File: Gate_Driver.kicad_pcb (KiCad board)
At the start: 2 copper layers, 110.3 x 47.3 mm, 23 parts

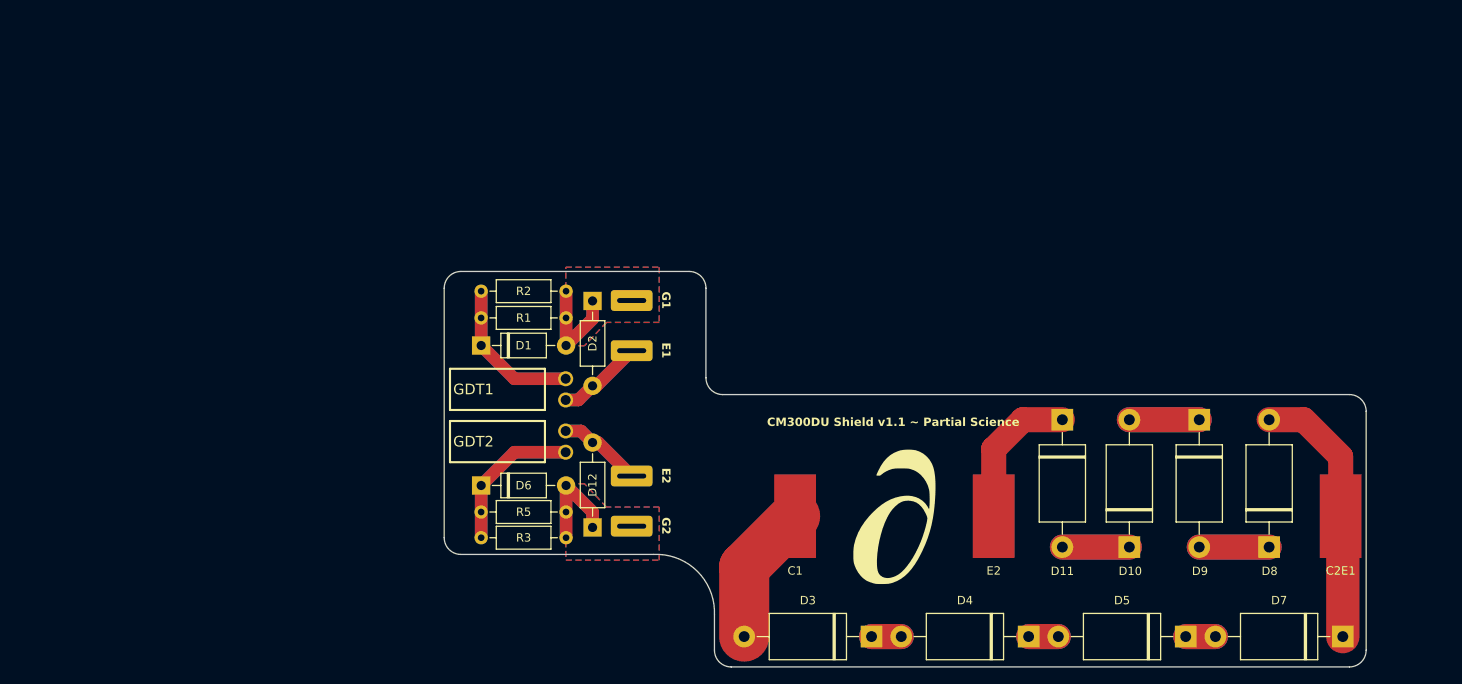
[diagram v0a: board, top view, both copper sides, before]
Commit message: Design done with smaller cap
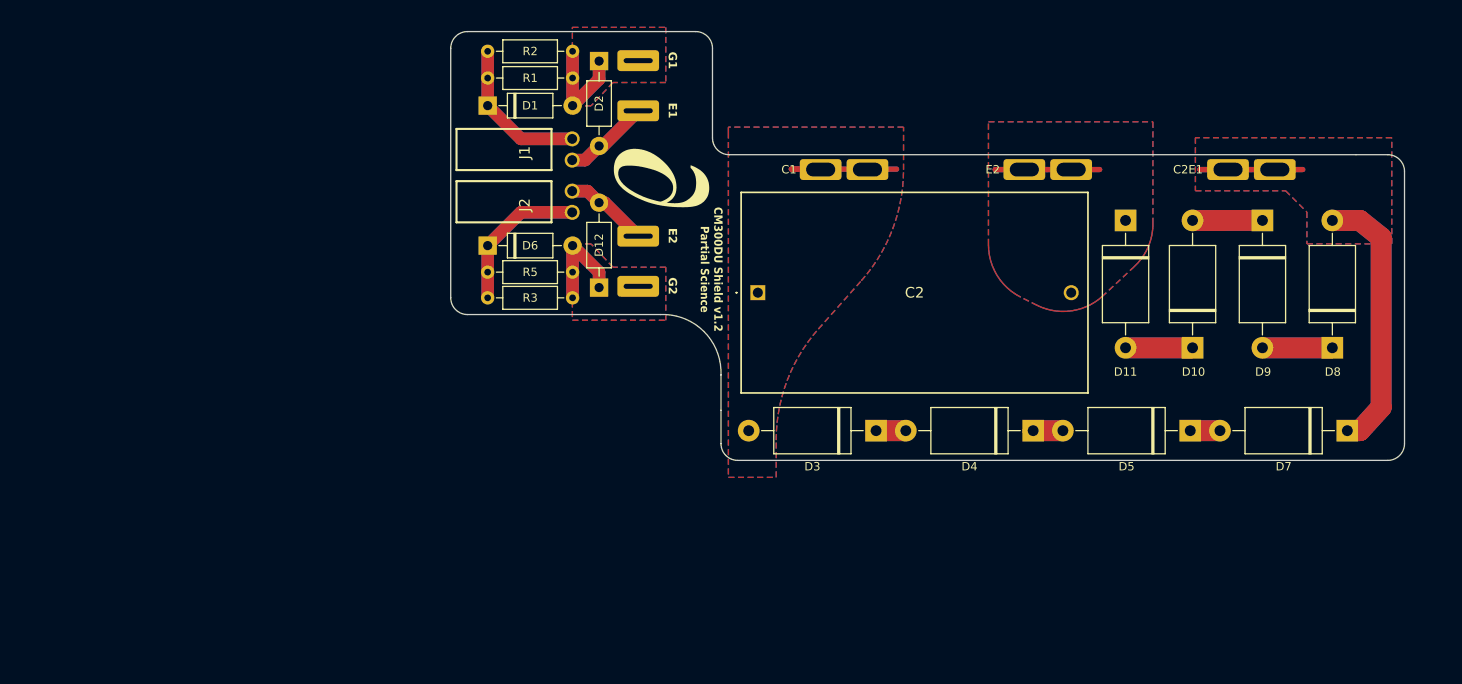
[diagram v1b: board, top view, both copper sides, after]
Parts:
- added C2: B32776T1275K000, SamacSys_Parts:B32776T1275K000, F.Cu at (121.8, 106.7)
- C1, C2E1, E2: footprint Connector_Wire:SolderWirePad_1x01_SMD_5x10mm -> Library:Custom CM300DU Terminal Connector
- D12, D2: value D_Zener -> P6KE30CA
- moved G*** 48.9 mm to (110.3, 93.0), turned to -90 degrees
- moved C2E1 42.8 mm to (180.8, 91.9)
- moved E2 42.0 mm to (156.5, 91.9)
- moved C1 41.9 mm to (132.1, 91.9)
- moved D12 28.7 mm to (102.8, 106.1)
- moved R5 28.7 mm to (89.5, 104.2)
- moved D1 28.7 mm to (89.5, 84.3)
- moved D2 28.7 mm to (102.8, 79.0)
- moved D6 28.7 mm to (89.5, 101.0)
- moved J1 28.7 mm to (93.9, 89.5)
- moved J2 28.7 mm to (93.9, 95.8)
- moved Q1 28.7 mm to (107.5, 92.4)
- moved R1 28.7 mm to (89.5, 81.0)
- moved R2 28.7 mm to (89.5, 77.8)
- moved R3 28.7 mm to (89.5, 107.3)
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- renumbered GDT1 to J1, GDT2 to J2
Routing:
- net Net-(C2E1-Pin_1): track 32.0 -> 0.00 mm
- net Net-(D11-A1): track 17.7 -> 0.00 mm
- net Net-(C1-Pin_1): track 16.9 -> 0.00 mm
- net Net-(D8-A1): track 16.7 -> 0.00 mm
- net Net-(D10-A2): track 16.7 -> 0.00 mm
- net Net-(D10-A1): track 16.0 -> 0.00 mm
- net Net-(D5-A1): track 7.11 -> 0.00 mm
- net Net-(D4-A1): track 7.11 -> 0.00 mm
- net Net-(D3-A1): track 7.11 -> 0.00 mm
- added copper zone on B.Cu, net Net-(C1-Pin_1)
- added copper zone on F.Cu, net Net-(C1-Pin_1)
- added copper zone on B.Cu, net Net-(C2E1-Pin_1)
- added copper zone on F.Cu, net Net-(C2E1-Pin_1)
- added copper zone on B.Cu, net Net-(D11-A1)
- added copper zone on F.Cu, net Net-(D11-A1)
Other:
- board size 110.3 x 47.3 mm -> 114.1 x 51.3 mm
- board text added: "CM300DU Shield v1.2 Partial Science"
- board text removed: "CM300DU Shield v1.1 ~ Partial Science"

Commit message: minor tweaks
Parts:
- removed C2: B32776T1275K000, SamacSys_Parts:B32776T1275K000
- moved G*** 62.4 mm to (48.3, 100.3), turned to 0 degrees
- moved C2E1 22.2 mm to (198.8, 105.0)
- moved C1 13.2 mm to (133.5, 105.0)
- moved E2 13.1 mm to (157.3, 105.0)
- moved D5 7.68 mm to (180.2, 119.4)
- moved D3 7.68 mm to (142.6, 119.4)
- moved D4 7.68 mm to (161.4, 119.4)
- moved D7 7.68 mm to (199.0, 119.4)
- moved D1 6.48 mm to (95.9, 84.6)
- moved D12 6.48 mm to (109.3, 106.4)
- moved D2 6.48 mm to (109.3, 79.3)
- moved D6 6.48 mm to (95.9, 101.4)
- moved R1 6.48 mm to (95.9, 81.3)
- moved R2 6.48 mm to (95.9, 78.1)
- moved R3 6.48 mm to (95.9, 107.6)
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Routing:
- net Net-(C2E1-Pin_1): track 0.00 -> 32.0 mm
- net Net-(D11-A1): track 0.00 -> 17.7 mm
- net Net-(C1-Pin_1): track 0.00 -> 16.9 mm
- net Net-(D8-A1): track 0.00 -> 16.7 mm
- net Net-(D10-A2): track 0.00 -> 16.7 mm
- net Net-(D10-A1): track 0.00 -> 16.0 mm
- net Net-(D4-A1): track 0.00 -> 7.11 mm
- net Net-(D3-A1): track 0.00 -> 7.11 mm
- net Net-(D5-A1): track 0.00 -> 7.11 mm
- removed copper zone on B.Cu, net Net-(C1-Pin_1)
- removed copper zone on F.Cu, net Net-(C1-Pin_1)
- removed copper zone on B.Cu, net Net-(C2E1-Pin_1)
- removed copper zone on F.Cu, net Net-(C2E1-Pin_1)
- removed copper zone on B.Cu, net Net-(D11-A1)
- removed copper zone on F.Cu, net Net-(D11-A1)
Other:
- board size 114.1 x 51.3 mm -> 110.3 x 47.3 mm
- board text added: "CM300DU Shield v1.1 ~ Partial Science"
- board text removed: "CM300DU Shield v1.2 Partial Science"

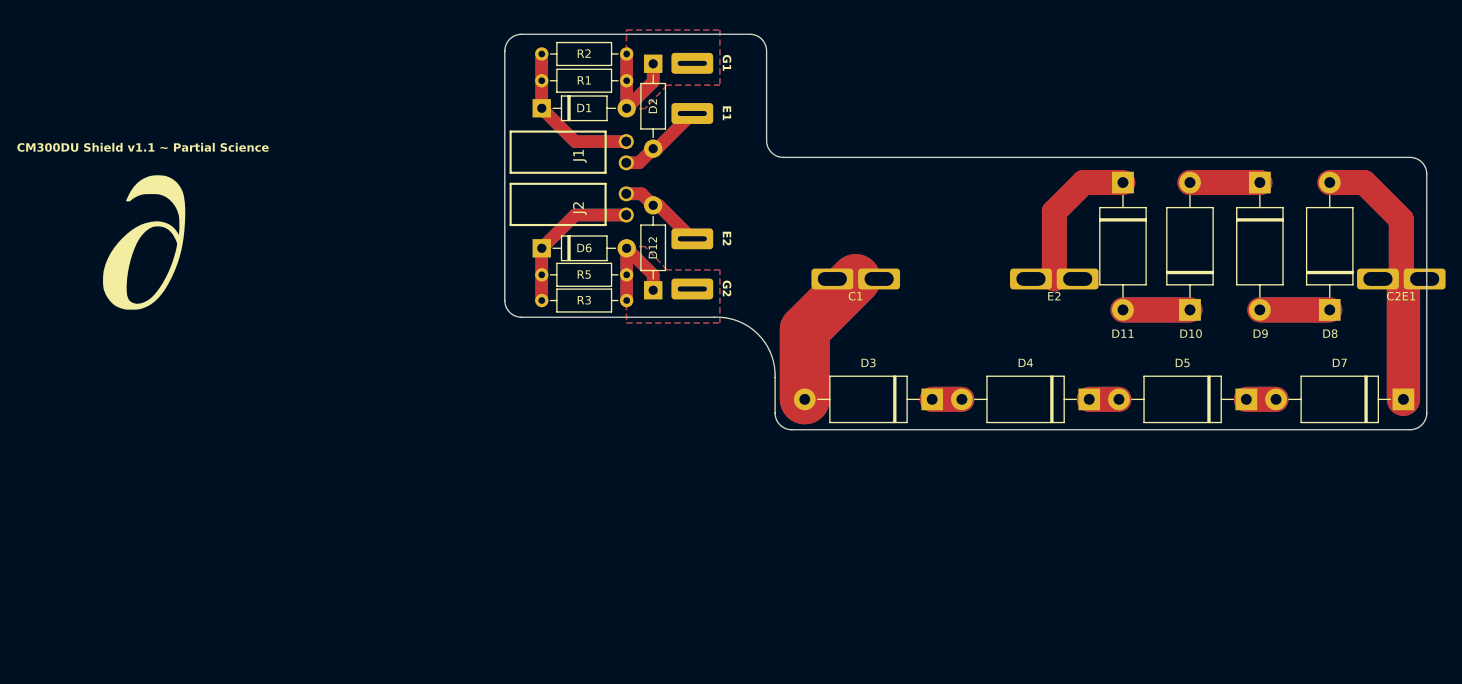
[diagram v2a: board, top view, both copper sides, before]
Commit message: Added pots and re-routed
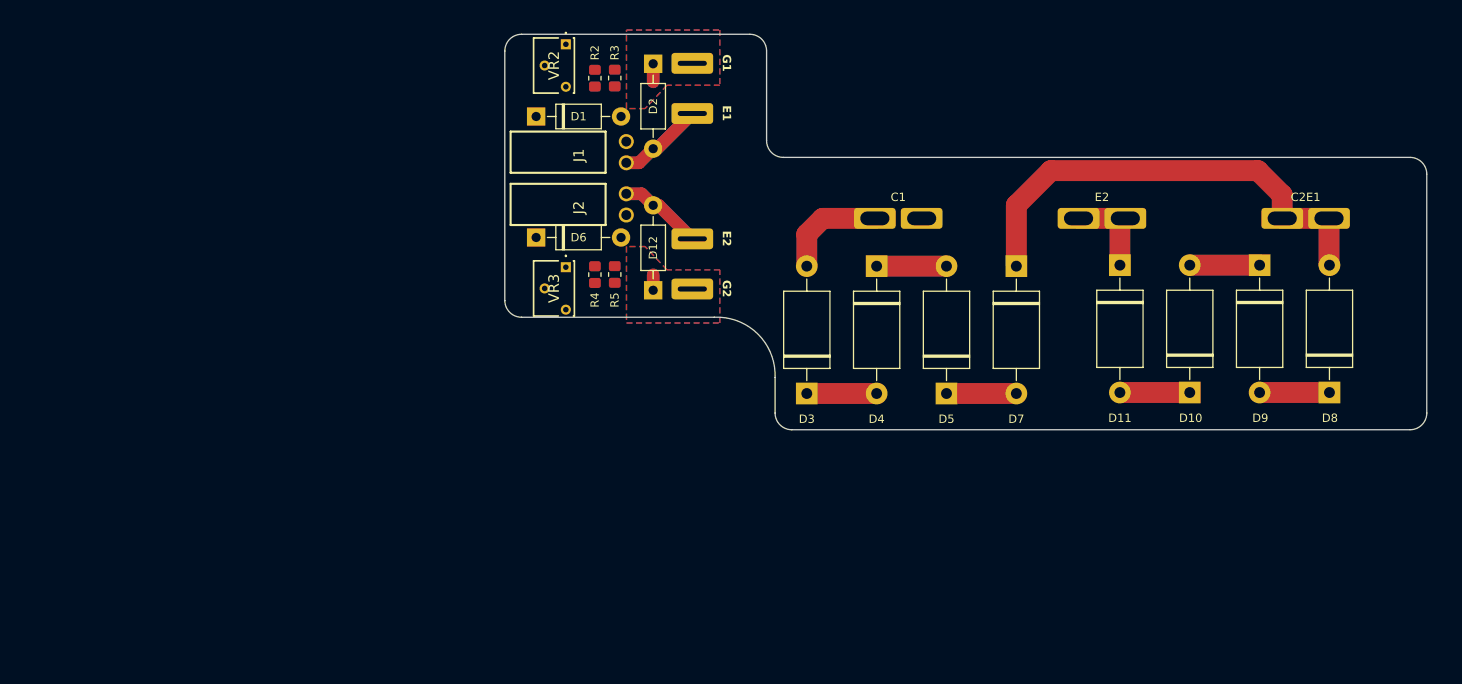
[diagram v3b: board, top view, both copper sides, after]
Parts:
- removed G***: LOGO, LOGO
- removed R1: 5.1, Resistor_THT:R_Axial_DIN0207_L6.3mm_D2.5mm_P10.16mm_Horizontal
- added R4: R, Resistor_SMD:R_0805_2012Metric_Pad1.20x1.40mm_HandSolder, F.Cu at (102.3, 104.5)
- added VR2: 3362X-1-100LF, SamacSys_Parts:3362X1100LF, F.Cu at (98.8, 77.0)
- added VR3: 3362X-1-100LF, SamacSys_Parts:3362X1100LF, F.Cu at (98.8, 103.6)
- R2, R3: footprint Resistor_THT:R_Axial_DIN0207_L6.3mm_D2.5mm_P10.16mm_Horizontal -> Resistor_SMD:R_0805_2012Metric_Pad1.20x1.40mm_HandSolder
- R5: value 5.1 -> R; footprint Resistor_THT:R_Axial_DIN0207_L6.3mm_D2.5mm_P10.16mm_Horizontal -> Resistor_SMD:R_0805_2012Metric_Pad1.20x1.40mm_HandSolder
- moved D7 49.0 mm to (152.7, 103.5), turned to -90 degrees
- moved D5 35.9 mm to (144.4, 118.7), turned to 90 degrees
- moved D4 30.0 mm to (136.0, 103.5), turned to -90 degrees
- moved R3 28.0 mm to (104.7, 81.0), turned to 90 degrees
- moved D3 15.0 mm to (127.6, 118.7), turned to 90 degrees
- moved C2E1 13.6 mm to (187.3, 97.8)
- moved D11 9.89 mm to (165.1, 103.4)
- moved D8 9.89 mm to (190.2, 118.6)
- moved D9 9.89 mm to (181.8, 103.4)
- moved D10 9.89 mm to (173.5, 118.6)
- moved E2 9.22 mm to (162.9, 97.8)
- moved C1 8.86 mm to (138.6, 97.8)
- moved R5 8.73 mm to (104.7, 104.5), turned to -90 degrees
- moved R2 6.98 mm to (102.3, 81.0), turned to 90 degrees
- moved D6 1.46 mm to (95.2, 100.1)
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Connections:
- R3 pad 1: Net-(D6-K) -> Net-(D1-K)
- R3 pad 2: Net-(D12-K) -> Net-(D1-A)
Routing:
- net Net-(D1-K): track 36.5 -> 0.00 mm
- net Net-(D6-K): track 36.0 -> 0.00 mm
- net Net-(C2E1-Pin_1): track 32.0 -> 56.0 mm
- net Net-(D1-A): track 26.3 -> 4.32 mm
- net Net-(D12-K): track 25.2 -> 3.70 mm
- net Net-(D10-A2): track 16.7 -> 8.36 mm
- net Net-(D8-A1): track 16.7 -> 8.36 mm
- net Net-(D10-A1): track 16.0 -> 8.36 mm
- net Net-(D11-A1): track 17.7 -> 11.5 mm
- net Net-(C1-Pin_1): track 16.9 -> 12.7 mm
- net Net-(D5-A1): track 7.11 -> 8.36 mm
- net Net-(D3-A1): track 7.11 -> 8.36 mm
- net Net-(D4-A1): track 7.11 -> 8.36 mm
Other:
- board text removed: "CM300DU Shield v1.1 ~ Partial Science"

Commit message: Polish design and finish routing
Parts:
- added G***: LOGO, LOGO, F.Cu at (116.2, 93.3)
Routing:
- net Net-(C2E1-Pin_1): track 56.0 -> 112.1 mm
- net Net-(C1-Pin_1): track 12.7 -> 36.7 mm
- net Net-(D1-K): track 0.00 -> 22.9 mm
- net Net-(D6-K): track 0.00 -> 22.8 mm
- net Net-(D12-K): track 3.70 -> 26.3 mm
- net Net-(D1-A): track 4.32 -> 26.1 mm
- net Net-(D2-A): track 20.7 -> 0.00 mm
- net Net-(D12-A): track 20.3 -> 0.00 mm
- net Net-(D11-A1): track 11.5 -> 22.9 mm
- net Net-(D8-A1): track 8.36 -> 16.7 mm
- net Net-(D10-A1): track 8.36 -> 16.7 mm
- net Net-(D3-A1): track 8.36 -> 16.7 mm
- net Net-(D5-A1): track 8.36 -> 16.7 mm
- net Net-(D4-A1): track 8.36 -> 16.7 mm
- net Net-(D10-A2): track 8.36 -> 16.7 mm
- added copper zone on B.Cu, net Net-(D12-A)
- added copper zone on B.Cu, net Net-(D2-A)
- removed copper zone on B.Cu, net Net-(D1-A)
- removed copper zone on F.Cu, net Net-(D1-A)
- removed copper zone on B.Cu, net Net-(D12-K)
- removed copper zone on F.Cu, net Net-(D12-K)
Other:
- board text added: "CM300DU Shield v1.3"
- board text added: "Made By Partial Science"

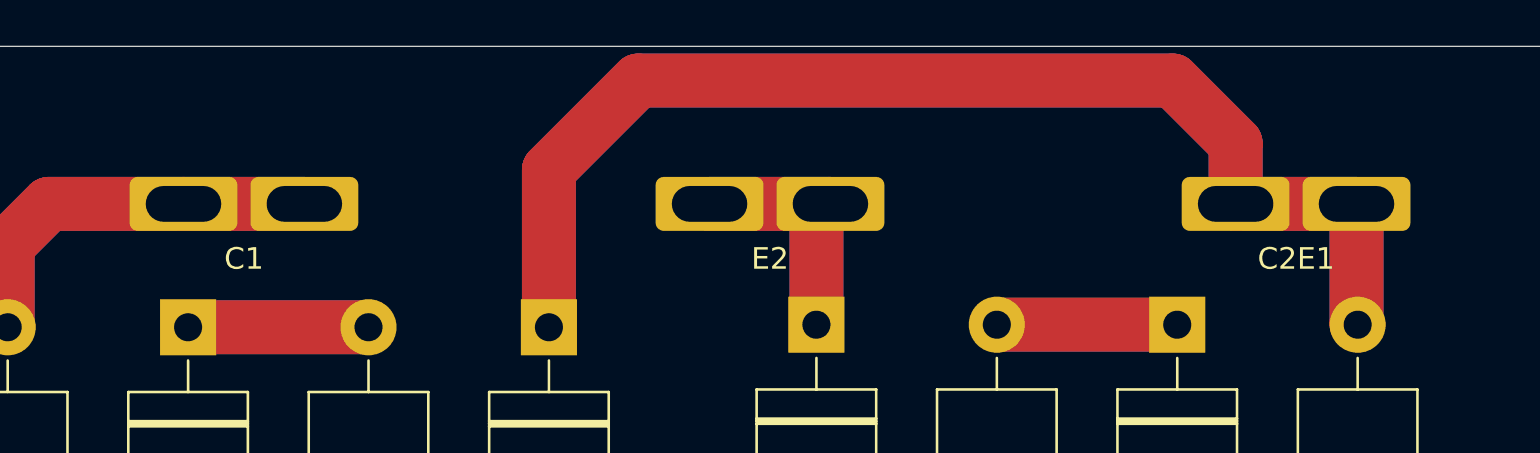
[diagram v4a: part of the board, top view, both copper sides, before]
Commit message: Clean up bom and minor PCB changes
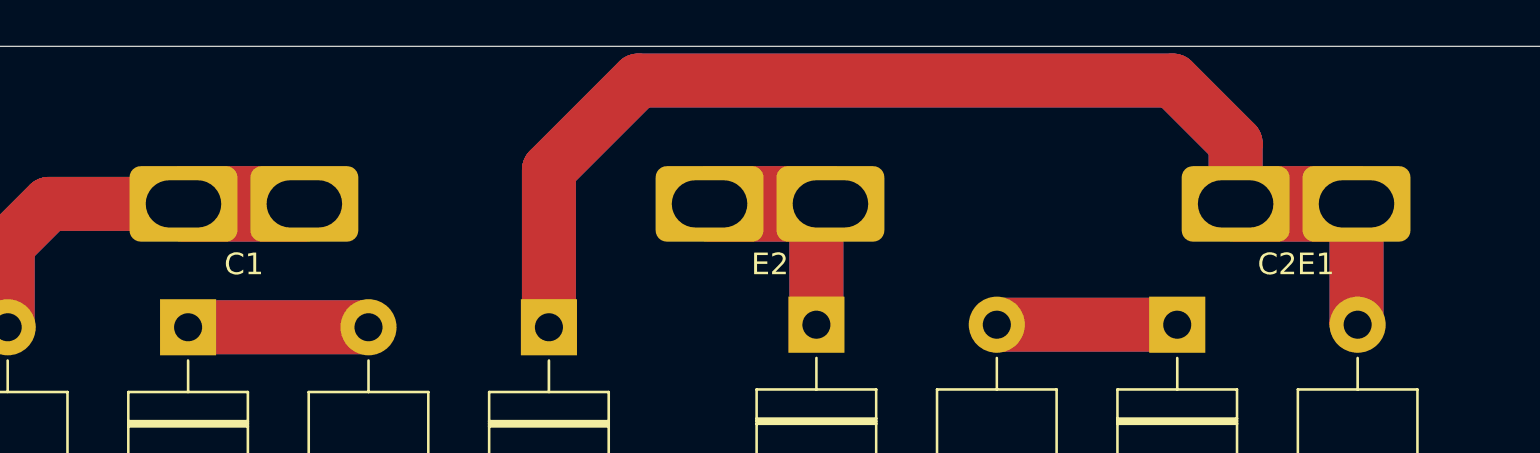
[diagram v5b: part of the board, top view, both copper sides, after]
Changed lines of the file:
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@@
 		(at 138.578898 97.79)
 		(property "Reference" "C1"
-			(at 0 2.54 0)
+			(at 0 2.794 0)
 			(unlocked yes)
 			(layer "F.SilkS")
@@
 		(attr smd)
 		(fp_text user "${REFERENCE}"
-			(at 0 2.54 0)
+			(at 0 2.794 0)
 			(unlocked yes)
 			(layer "F.Fab")
@@
 		(pad "1" thru_hole roundrect
 			(at -2.8 0)
-			(size 5 2.5)
-			(drill oval 3.5 1.66)
+			(size 5 3.5)
+			(drill oval 3.5 2.19)
 			(layers "*.Cu" "*.Mask")
 			(remove_unused_layers no)
@@
 		(pad "1" thru_hole roundrect
 			(at 2.8 0)
-			(size 5 2.5)
-			(drill oval 3.5 1.66)
+			(size 5 3.5)
+			(drill oval 3.5 2.19)
 			(layers "*.Cu" "*.Mask")
 			(remove_unused_layers no)
@@
 		)
 		(embedded_fonts no)
+		(model "${KIPRJMOD}/Custom-Connector.stp"
+			(offset
+				(xyz -24.38 5.05 -24)
+			)
+			(scale
+				(xyz 1 1 1)
+			)
+			(rotate
+				(xyz -0 -0 -180)
+			)
+		)
 	)
 	(footprint "LOGO"
@@
 		(at 162.95 97.79)
 		(property "Reference" "E2"
-			(at 0 2.54 0)
+			(at 0 2.794 0)
 			(unlocked yes)
 			(layer "F.SilkS")
@@
 		(attr smd)
 		(fp_text user "${REFERENCE}"
-			(at 0 2.54 0)
+			(at 0 2.794 0)
 			(unlocked yes)
 			(layer "F.Fab")
@@
 		(pad "1" thru_hole roundrect
 			(at -2.8 0)
-			(size 5 2.5)
-			(drill oval 3.5 1.66)
+			(size 5 3.5)
+			(drill oval 3.5 2.19)
 			(layers "*.Cu" "*.Mask")
 			(remove_unused_layers no)
@@
 		(pad "1" thru_hole roundrect
 			(at 2.8 0)
-			(size 5 2.5)
-			(drill oval 3.5 1.66)
+			(size 5 3.5)
+			(drill oval 3.5 2.19)
 			(layers "*.Cu" "*.Mask")
 			(remove_unused_layers no)
@@
 		)
 		(embedded_fonts no)
+		(model "${KIPRJMOD}/Custom-Connector.stp"
+			(offset
+				(xyz -24.38 5.05 -24)
+			)
+			(scale
+				(xyz 1 1 1)
+			)
+			(rotate
+				(xyz -0 -0 -180)
+			)
+		)
 	)
 	(footprint "SamacSys_Parts:3362X1100LF"
@@
 		(at 187.321102 97.79)
 		(property "Reference" "C2E1"
-			(at 0 2.54 0)
+			(at 0 2.794 0)
 			(unlocked yes)
 			(layer "F.SilkS")
@@
 		(attr smd)
 		(fp_text user "${REFERENCE}"
-			(at 0 -2.54 0)
+			(at 0 2.794 0)
 			(unlocked yes)
 			(layer "F.Fab")
@@
 		(pad "1" thru_hole roundrect
 			(at -2.8 0)
-			(size 5 2.5)
-			(drill oval 3.5 1.66)
+			(size 5 3.5)
+			(drill oval 3.5 2.19)
 			(layers "*.Cu" "*.Mask")
 			(remove_unused_layers no)
@@
 		(pad "1" thru_hole roundrect
 			(at 2.8 0)
-			(size 5 2.5)
-			(drill oval 3.5 1.66)
+			(size 5 3.5)
+			(drill oval 3.5 2.19)
 			(layers "*.Cu" "*.Mask")
 			(remove_unused_layers no)
@@
 		)
 		(embedded_fonts no)
+		(model "${KIPRJMOD}/Custom-Connector.stp"
+			(offset
+				(xyz -24.38 5.05 -24)
+			)
+			(scale
+				(xyz 1 1 1)
+			)
+			(rotate
+				(xyz -0 -0 -180)
+			)
+		)
 	)
 	(footprint "Diode_THT:D_DO-41_SOD81_P10.16mm_Horizontal"
@@
 		(start 135.778898 97.79)
 		(end 141.378898 97.79)
-		(width 2.5)
+		(width 3.5)
 		(layer "F.Cu")
 		(net 9)
@@
 		(start 141.378898 97.79)
 		(end 135.778898 97.79)
-		(width 2.5)
+		(width 3.5)
 		(layer "B.Cu")
 		(net 9)
@@
 		(start 190.121102 97.79)
 		(end 184.521102 97.79)
-		(width 2.5)
+		(width 3.5)
 		(layer "F.Cu")
 		(net 11)
@@
 		(start 190.121102 97.79)
 		(end 184.521102 97.79)
-		(width 2.5)
+		(width 3.5)
 		(layer "B.Cu")
 		(net 11)
@@
 		(start 160.15 97.79)
 		(end 165.75 97.79)
-		(width 2.5)
+		(width 3.5)
 		(layer "F.Cu")
 		(net 13)
@@
 		(start 165.75 97.79)
 		(end 160.15 97.79)
-		(width 2.5)
+		(width 3.5)
 		(layer "B.Cu")
 		(net 13)
